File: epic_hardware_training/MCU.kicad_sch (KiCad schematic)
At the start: 2 parts, among them J1 RJ45_LED_Shielded, U1 Teensy4.1_DEV-16771

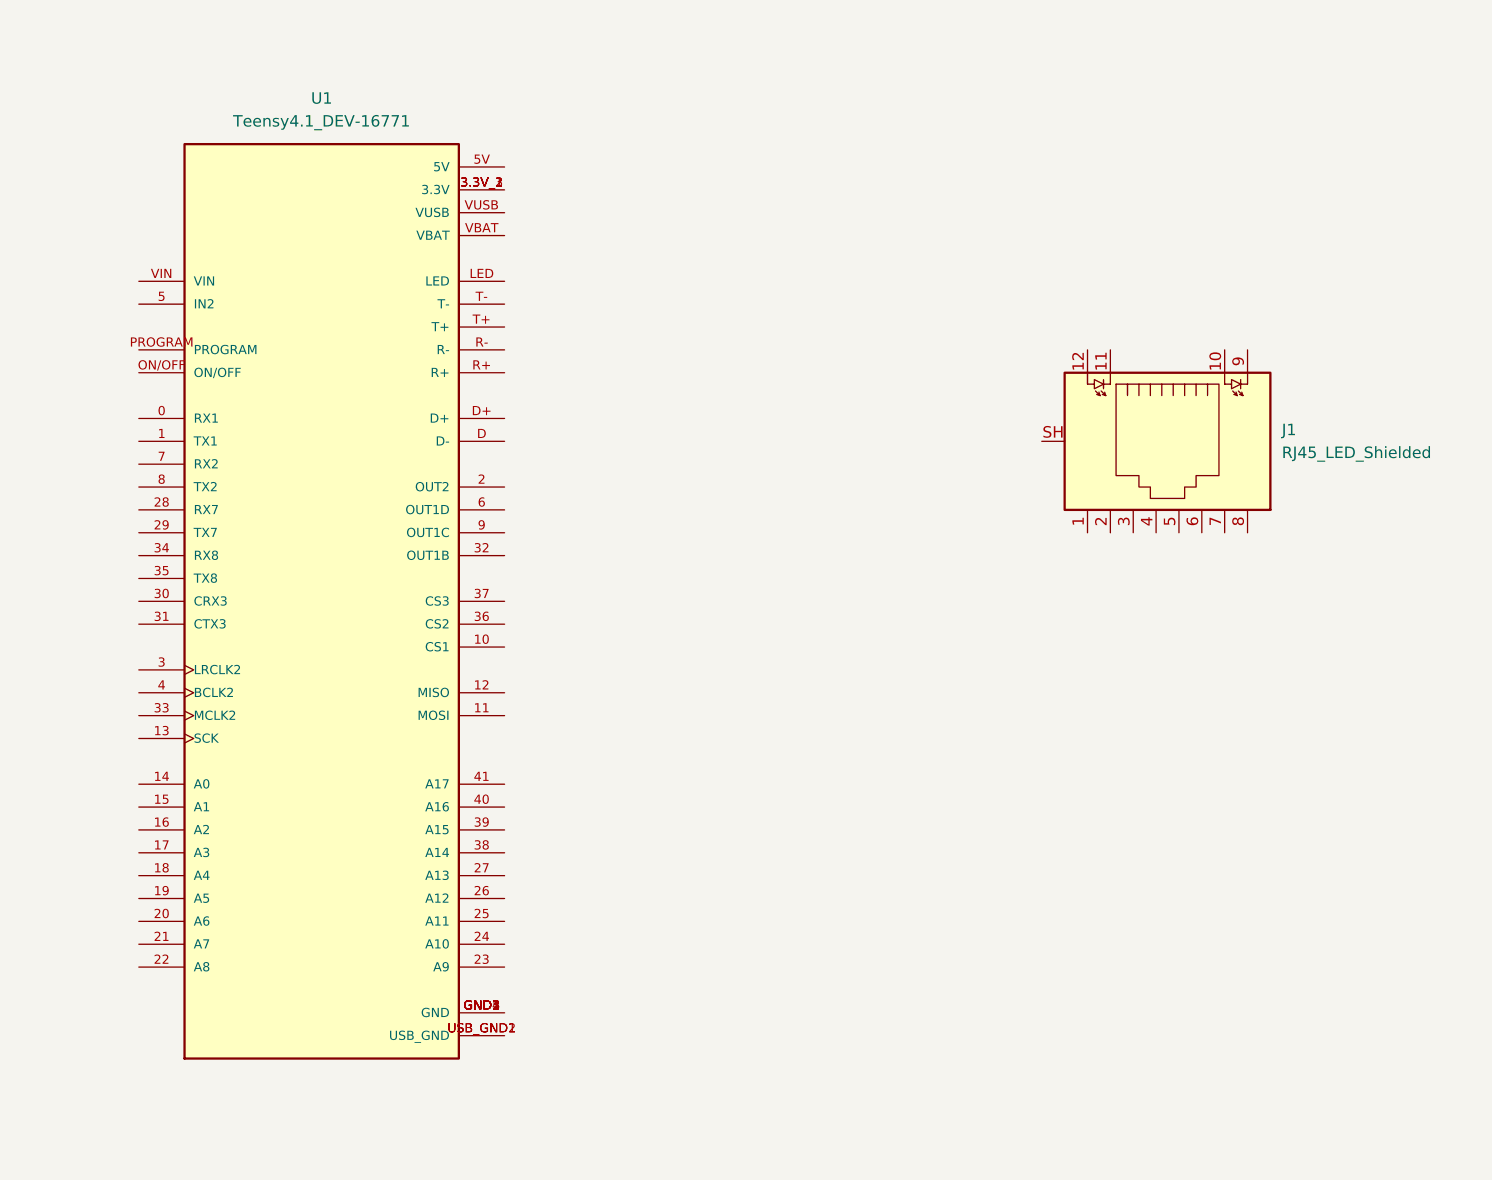
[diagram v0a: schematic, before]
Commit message: add ethernet
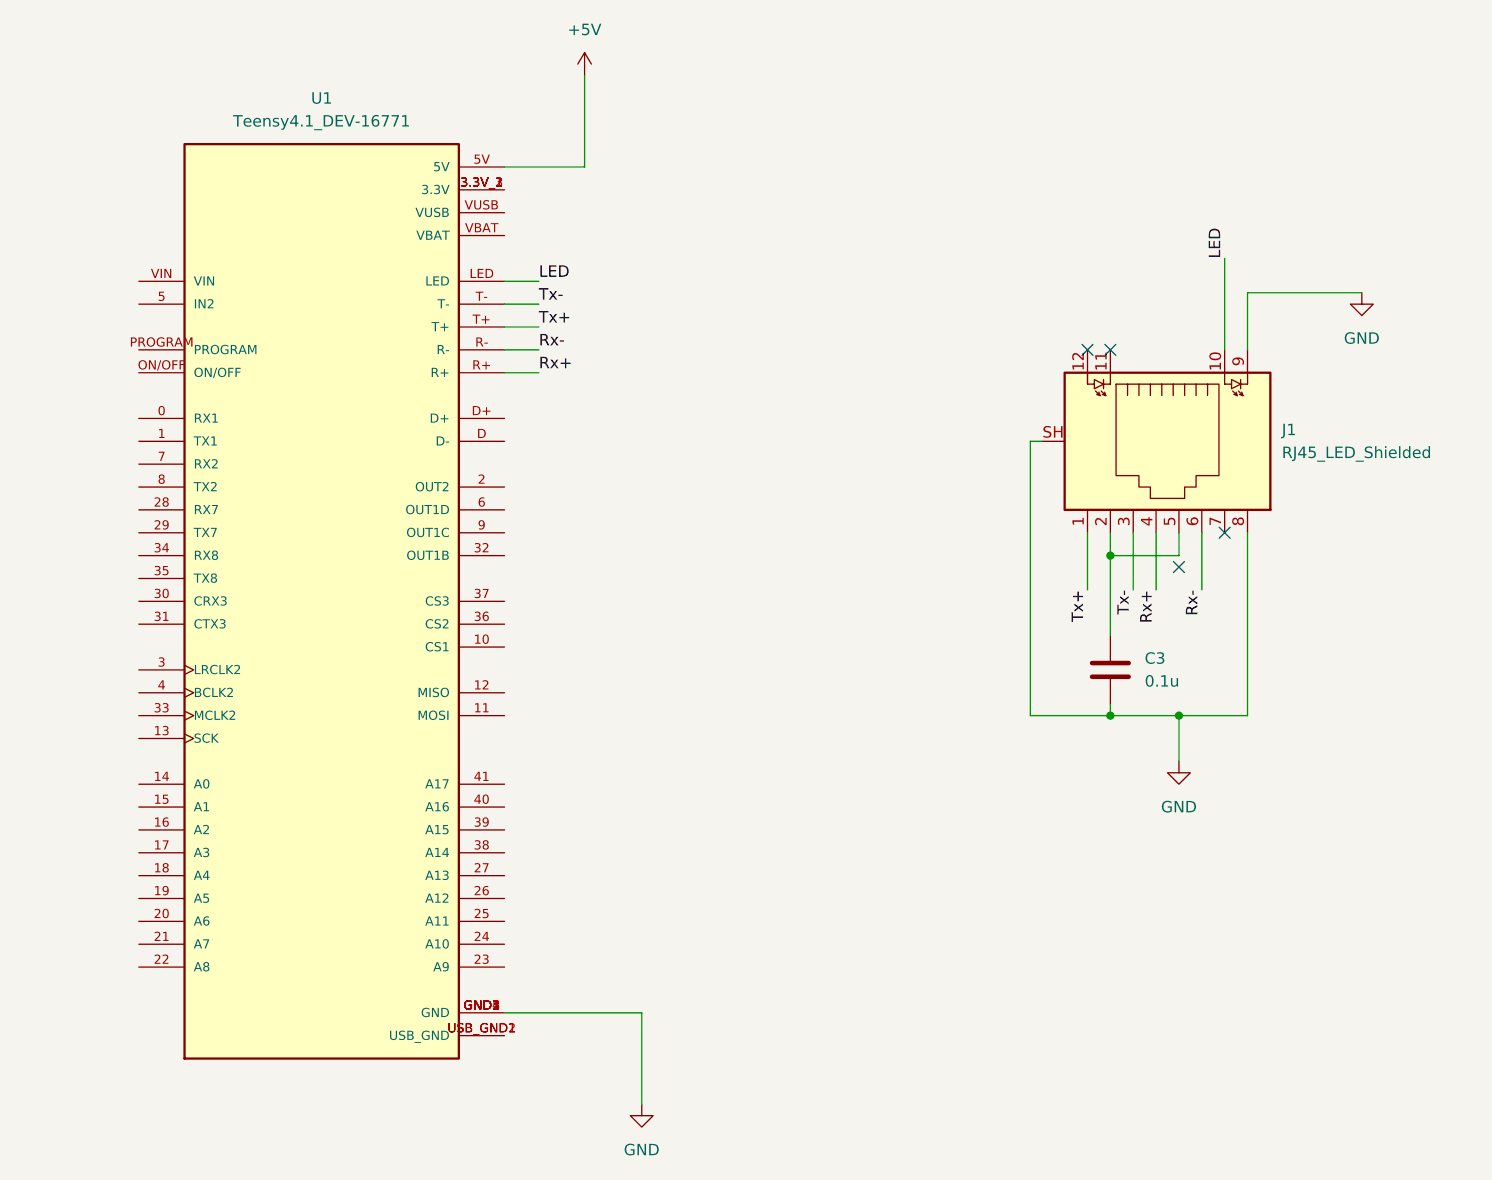
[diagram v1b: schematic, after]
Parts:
- added C3: 0.1u, symbol Device:C
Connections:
- net Tx+: now reaches J1.1
- net Tx+: now also U1.T+
- net LED: now reaches J1.10
- net LED: now also U1.LED
- net at J1.2: now also J1.5, C3.1
- net Tx-: now reaches J1.3
- net Tx-: now also U1.T-
- net Rx+: now reaches J1.4
- net Rx+: now also U1.R+
- net Rx-: now reaches J1.6
- net Rx-: now also U1.R-
- net GND: now reaches J1.8
- net GND: now also J1.9, J1.SH, U1.GND1 (GND), U1.GND2 (GND), U1.GND3 (GND), U1.GND4 (GND), U1.GND5 (GND), C3.2
- net +5V: now reaches U1.5V
- no-connect marks 0 -> 4

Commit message: complete schematic
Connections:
- net STBY: now reaches U1.2 (OUT2)
- net TX1: now reaches U1.22 (A8)
- net CRX1: now reaches U1.23 (A9)
- net +3V3: now reaches U1.3.3V_1 (3.3V), U1.3.3V_2 (3.3V), U1.3.3V_3 (3.3V)
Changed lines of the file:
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@@
+	(wire
+		(pts
+			(xy 95.25 43.18) (xy 113.03 43.18)
+		)
+		(stroke
+			(width 0)
+			(type default)
+		)
+	)
 	(wire
 		(pts
@@
 	(wire
 		(pts
+			(xy 113.03 31.75) (xy 113.03 43.18)
+		)
+		(stroke
+			(width 0)
+			(type default)
+		)
+	)
+	(wire
+		(pts
 			(xy 95.25 53.34) (xy 99.06 53.34)
 		)
@@
 	(wire
 		(pts
+			(xy 95.25 129.54) (xy 102.87 129.54)
+		)
+		(stroke
+			(width 0)
+			(type default)
+		)
+	)
+	(wire
+		(pts
 			(xy 177.8 81.28) (xy 177.8 101.6)
 		)
@@
 	(wire
 		(pts
+			(xy 95.25 76.2) (xy 99.06 76.2)
+		)
+		(stroke
+			(width 0)
+			(type default)
+		)
+	)
+	(wire
+		(pts
 			(xy 172.72 81.28) (xy 172.72 87.63)
 		)
@@
 		(pts
 			(xy 95.25 40.64) (xy 104.14 40.64)
+		)
+		(stroke
+			(width 0)
+			(type default)
+		)
+	)
+	(wire
+		(pts
+			(xy 46.99 129.54) (xy 54.61 129.54)
 		)
 		(stroke
@@
 			)
 			(justify left bottom)
+		)
+	)
+	(hierarchical_label "TX1"
+		(shape output)
+		(at 46.99 129.54 180)
+		(effects
+			(font
+				(size 1.27 1.27)
+			)
+			(justify right)
+		)
+	)
+	(hierarchical_label "STBY"
+		(shape output)
+		(at 99.06 76.2 0)
+		(effects
+			(font
+				(size 1.27 1.27)
+			)
+			(justify left)
+		)
+	)
+	(hierarchical_label "CRX1"
+		(shape input)
+		(at 102.87 129.54 0)
+		(effects
+			(font
+				(size 1.27 1.27)
+			)
+			(justify left)
 		)
 	)
@@
 					(unit 1)
 				)
+			)
+		)
+	)
+	(symbol
+		(lib_id "power:+3V3")
+		(at 113.03 31.75 0)
+		(unit 1)
+		(exclude_from_sim no)
+		(in_bom yes)
+		(on_board yes)
+		(dnp no)
+		(fields_autoplaced yes)
+		(property "Reference" "#PWR016"
+			(at 113.03 35.56 0)
+			(effects
+				(font
+					(size 1.27 1.27)
+				)
+				(hide yes)
+			)
+		)
+		(property "Value" "+3V3"
+			(at 113.03 26.67 0)
+			(effects
+				(font
+					(size 1.27 1.27)
+				)
+			)
+		)
+		(property "Footprint" ""
+			(at 113.03 31.75 0)
+			(effects
+				(font
+					(size 1.27 1.27)
+				)
+				(hide yes)
+			)
+		)
+		(property "Datasheet" ""
+			(at 113.03 31.75 0)
+			(effects
+				(font
+					(size 1.27 1.27)
+				)
+				(hide yes)
+			)
+		)
+		(property "Description" "Power symbol creates a global label with name \"+3V3\""
+			(at 113.03 31.75 0)
+			(effects
+				(font
+					(size 1.27 1.27)
+				)
+				(hide yes)
+			)
+		)
+		(pin "1"
+		)
+		(instances
+			(project ""
+				(path "/30ac4f03-b625-4332-b9e2-69de598ec1a0/5ff024d1-978c-48f0-8ac6-753b22a31855"
+					(reference "#PWR016")
+					(unit 1)
+				)
